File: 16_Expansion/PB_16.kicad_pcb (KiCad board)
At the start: 2 copper layers, 148.6 x 75.6 mm, 57 parts, among them J1 String1, J10 String10, J11 String11, J12 String12, J13 String13, J14 String14, J15 String15, J16 String16, J17 Power In Left, J18 Power In Right, J19 Expansion Header, J2 String2, J3 String3, J4 String4, J5 String5, J6 String6, J7 String7, J8 String8, J9 String9, U1 SN74HCT245N, U2 SN74HCT245N

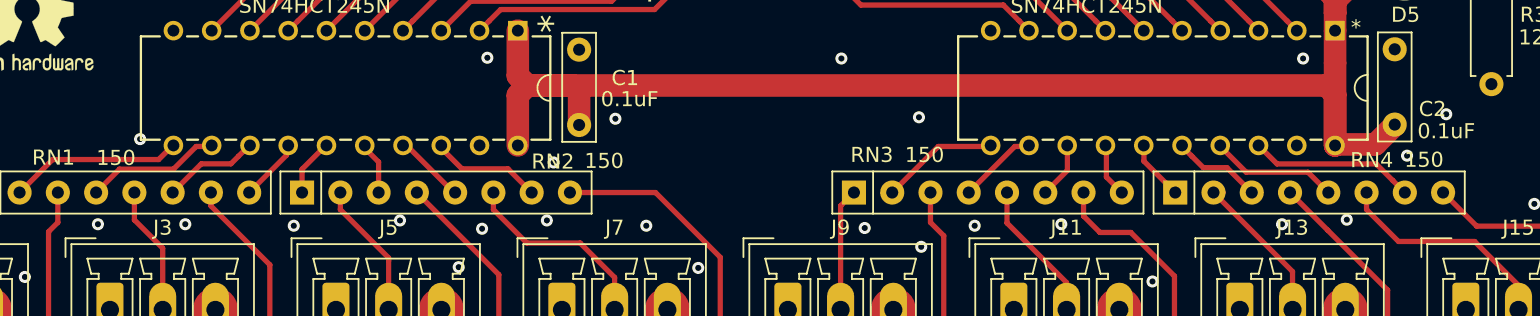
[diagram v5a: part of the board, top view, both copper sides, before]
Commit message: Updated Pixel Pixel resistor packs to 33ohms
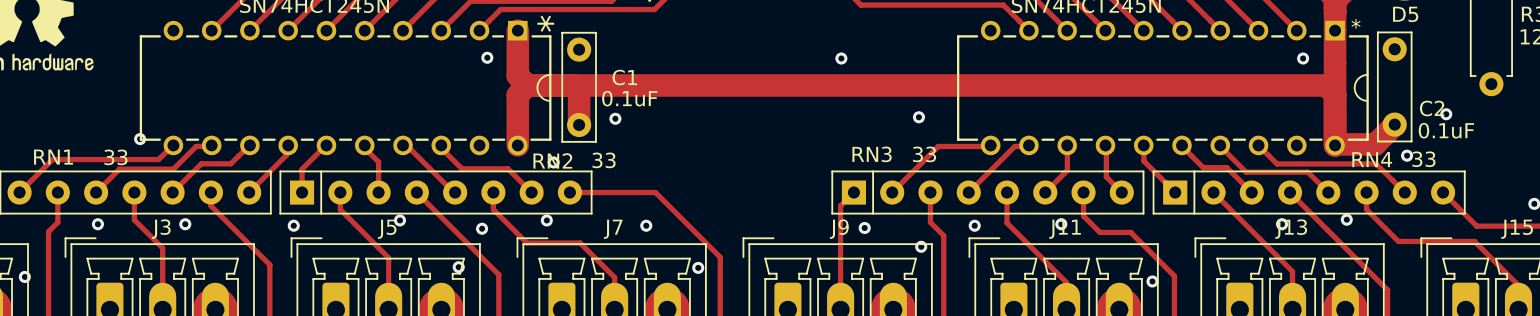
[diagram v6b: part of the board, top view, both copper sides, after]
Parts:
- RN1, RN2, RN3, RN4: value 150 -> 33

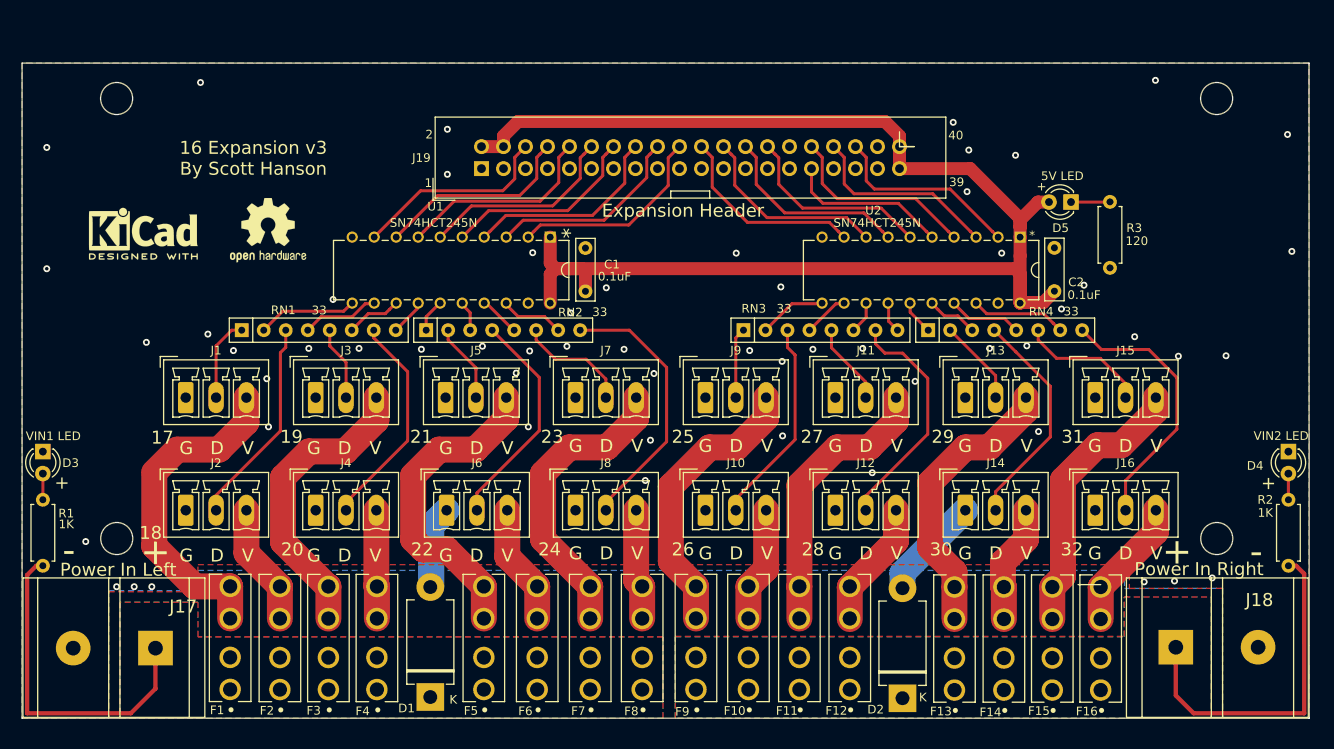
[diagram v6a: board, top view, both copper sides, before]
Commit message: added Falcon v4 Header Input
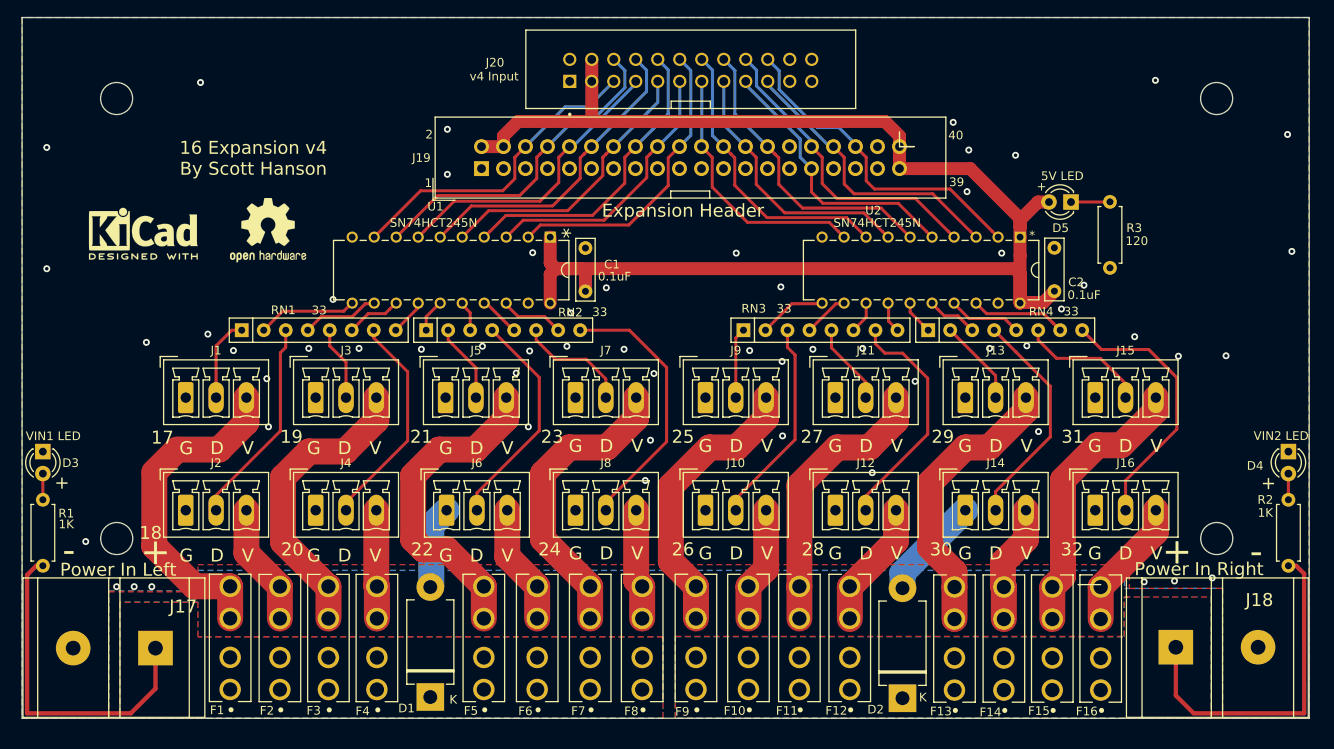
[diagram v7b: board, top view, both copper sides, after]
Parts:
- added J20: v4 Input, 302-S241:OST_302-S241, F.Cu at (147.4, 78.8)
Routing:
- net OUT32: track 22.4 -> 38.1 mm
- net OUT18: track 23.2 -> 38.8 mm
- net OUT17: track 23.3 -> 36.6 mm
- net OUT20: track 23.2 -> 36.4 mm
- net OUT30: track 22.6 -> 35.8 mm
- net OUT29: track 18.8 -> 32.0 mm
- net OUT28: track 22.6 -> 34.7 mm
- net OUT22: track 23.5 -> 35.7 mm
- net OUT24: track 23.7 -> 34.8 mm
- net OUT26: track 22.7 -> 33.8 mm
- net OUT31: track 23.1 -> 34.1 mm
- net OUT19: track 23.5 -> 34.4 mm
- net OUT21: track 23.0 -> 32.7 mm
- net OUT23: track 23.2 -> 31.8 mm
- net OUT27: track 22.6 -> 31.2 mm
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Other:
- board size 148.6 x 75.6 mm -> 148.6 x 80.9 mm
- board text added: "16 Expansion v4 By Scott Hanson"
- board text removed: "16 Expansion v3 By Scott Hanson"

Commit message: redid header placement and made PCB smaller again
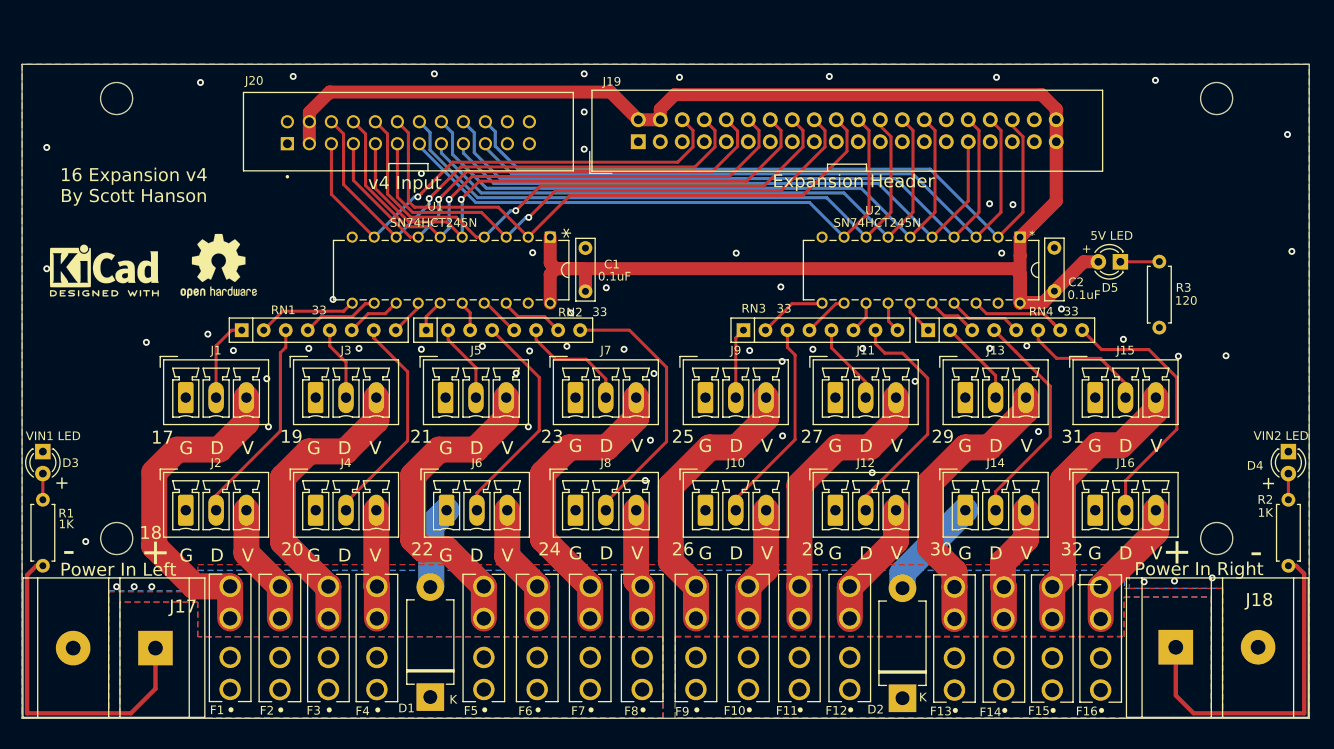
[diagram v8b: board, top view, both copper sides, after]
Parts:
- moved J20 33.4 mm to (114.8, 86.0)
- moved J19 18.4 mm to (141.3, 87.1)
- moved D5 8.95 mm to (197.0, 100.9)
- moved R3 8.95 mm to (201.5, 108.5)
- moved REF** 7.05 mm to (92.9, 101.4)
- moved REF** 6.19 mm to (79.7, 101.9)
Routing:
- net OUT30: track 35.8 -> 78.8 mm
- net OUT32: track 38.1 -> 81.0 mm
- net OUT31: track 34.1 -> 76.6 mm
- net OUT28: track 34.7 -> 76.3 mm
- net OUT27: track 31.2 -> 71.9 mm
- net OUT29: track 32.0 -> 72.0 mm
- net OUT26: track 33.8 -> 73.5 mm
- net OUT25: track 30.3 -> 68.9 mm
- net OUT24: track 34.8 -> 70.3 mm
- net OUT23: track 31.8 -> 65.4 mm, vias 0 -> 1
- net +5V: track 169.5 -> 202.0 mm
- net OUT21: track 32.7 -> 65.0 mm, vias 0 -> 1
- net OUT22: track 35.7 -> 66.9 mm, vias 0 -> 1
- net OUT20: track 36.4 -> 65.7 mm, vias 0 -> 1
- net OUT19: track 34.4 -> 60.4 mm, vias 0 -> 1
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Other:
- board size 148.6 x 80.9 mm -> 148.6 x 75.5 mm
- board text removed: "1"
- board text removed: "2"
- board text removed: "39"
- board text removed: "40"
